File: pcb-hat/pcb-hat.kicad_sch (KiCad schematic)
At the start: 32 parts, among them U1 INA219AxD, U3 AOZ6605PI-1

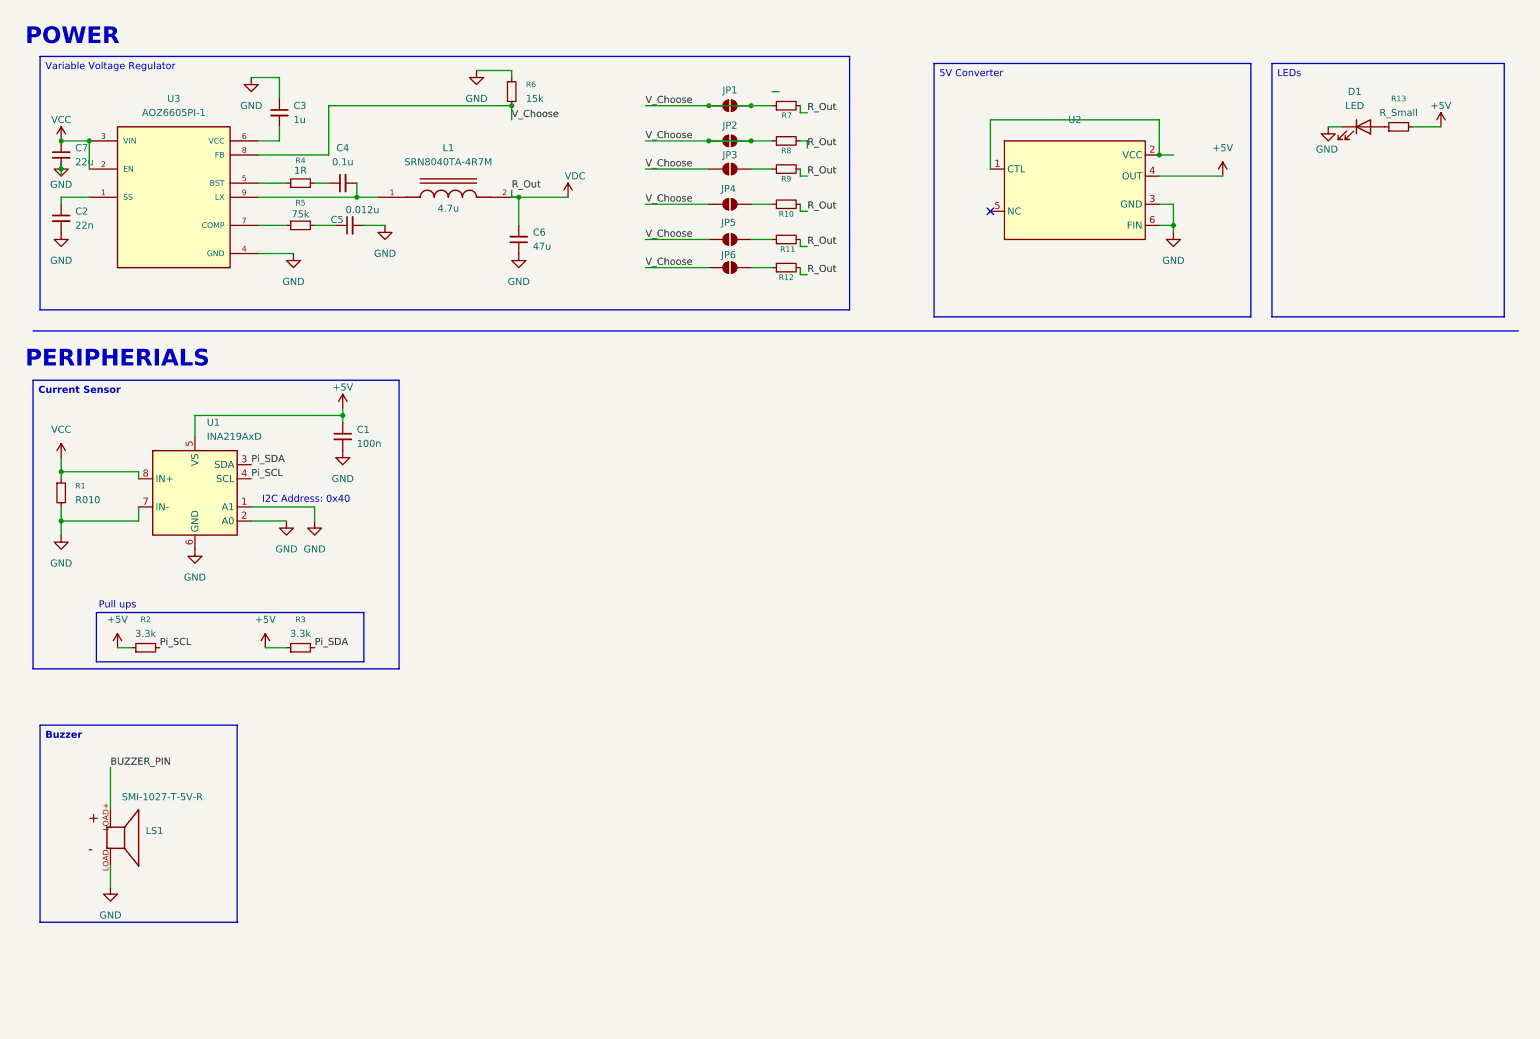
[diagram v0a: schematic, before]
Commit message: Add Pi, LED, Servo to the schematic
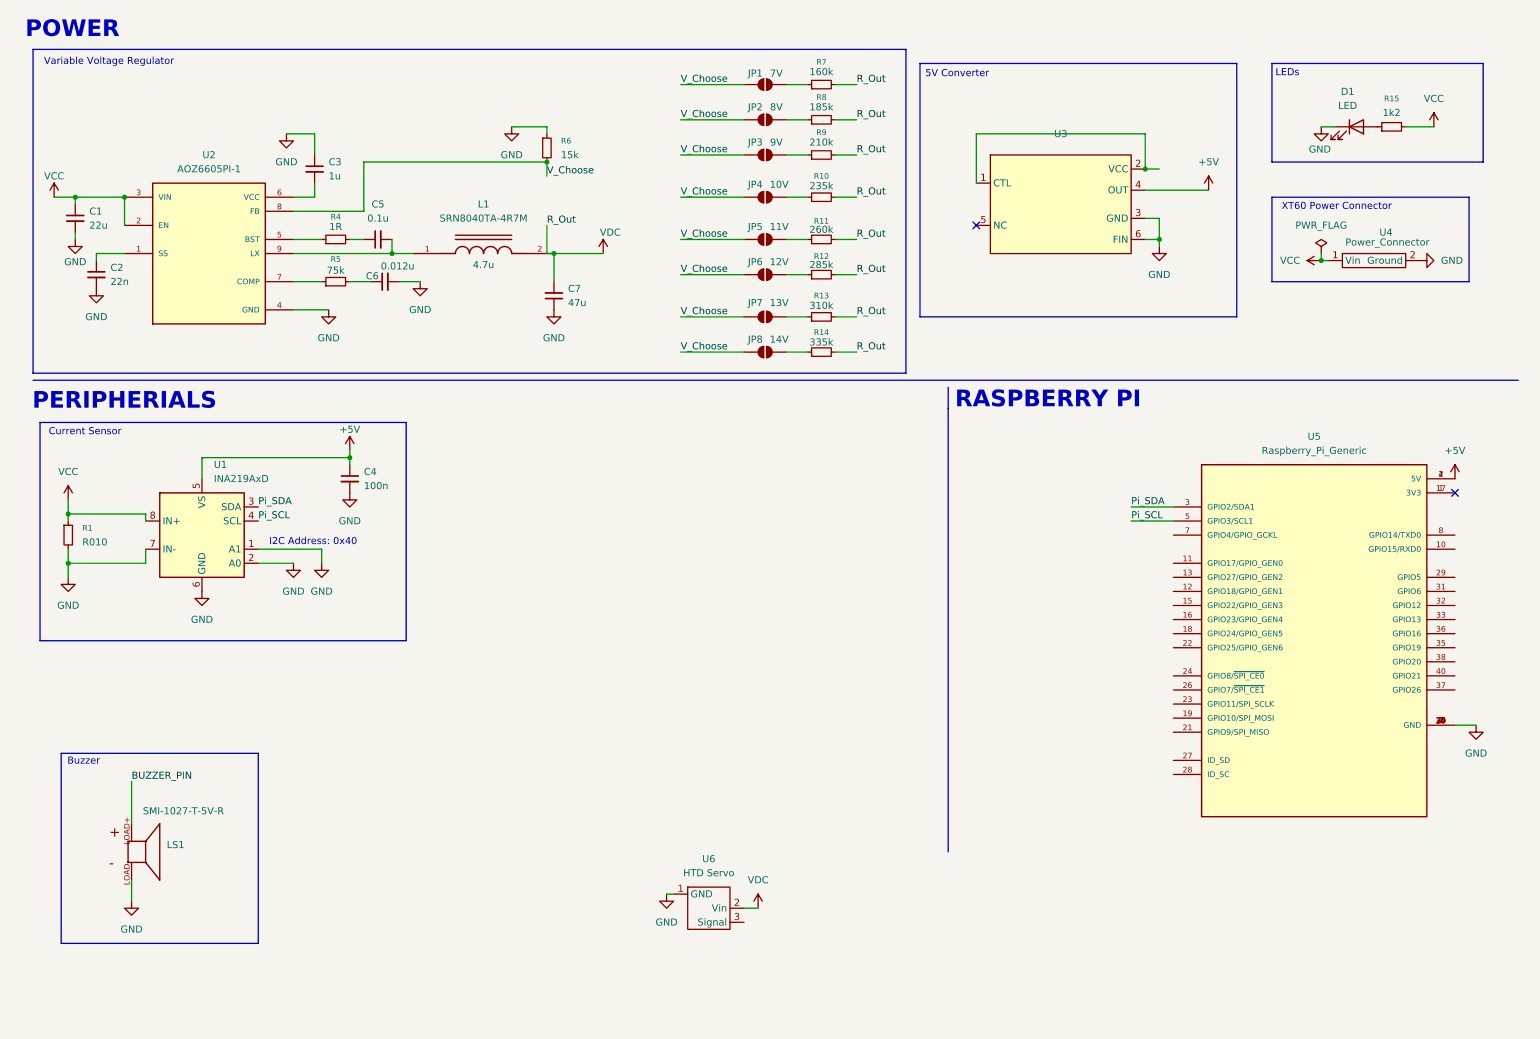
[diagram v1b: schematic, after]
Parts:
- removed R2, R3: 3.3k, Resistor_SMD:R_0603_1608Metric, symbol Device:R_Small
- added JP1, JP2: SolderJumper_2_Open, Jumper:SolderJumper-2_P1.3mm_Open_RoundedPad1.0x1.5mm, symbol Jumper:SolderJumper_2_Open
- added R7: 160k, Resistor_SMD:R_0201_0603Metric_Pad0.64x0.40mm_HandSolder, symbol Device:R_Small
- added R8: 185k, Resistor_SMD:R_0201_0603Metric_Pad0.64x0.40mm_HandSolder, symbol Device:R_Small
- added U4: Power_Connector, pi_hat:XT60, symbol PiHatComponents:XT60
- added U5: Raspberry_Pi_Generic, pcb_hat:Pi5Hat, symbol PiHatComponents:Raspberry_Pi_Generic
- added U6: HTD Servo, pcb_hat:Servo, symbol PiHatComponents:ServoPinHeader
- JP3: renamed from JP1; V_out (none) -> 9V
- JP4: renamed from JP2; V_out (none) -> 10V
- JP5: renamed from JP3; V_out (none) -> 11V
- JP6: renamed from JP4; V_out (none) -> 12V
- JP7: renamed from JP5; V_out (none) -> 13V
- JP8: renamed from JP6; V_out (none) -> 14V
- R15: renamed from R13; value R_Small -> 1k2
- renumbered C7 to C1, C1 to C4, C4 to C5, C5 to C6, C6 to C7, R8 to R10, R9 to R11, R10 to R12, R11 to R13, R12 to R14, R7 to R9, U3 to U2, U2 to U3
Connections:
- net +5V: now also U5.2 (5V), U5.4 (5V); no longer R15.2
- net GND: now also U4.2 (Ground), U5.20 (GND), U5.25 (GND), U5.30 (GND), U5.34 (GND), U5.39 (GND), U5.6 (GND), U5.9 (GND), U6.1 (GND)
- net Pi_SCL: now also U5.5 (GPIO3/SCL1)
- net Pi_SDA: now also U5.3 (GPIO2/SDA1)
- net VCC: now also R15.2, U4.1 (Vin)
- net VDC: now also R7.2, R8.2, U6.2 (Vin)
- net V_Choose: now also JP1.1 (A), JP2.1 (A); no longer JP3.2 (B), JP4.2 (B), R10.1, R9.1
- new net: JP4.2 (B), R10.1
- new net: U5.1 (3V3), U5.17 (3V3)
- new net: JP3.2 (B), R9.1
- new net: JP1.2 (B), R7.1
- new net: JP2.2 (B), R8.1
- no-connect marks 1 -> 2
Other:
- note added: "Buzzer"
- note added: "Current Sensor"
- note added: "LEDs"
- note added: "RASPBERRY PI"
- note added: "Variable Voltage Regulator"
- note added: "XT60 Power Connector"
- note removed: "Pull ups"
- moved on the sheet: C1, C2, C3, C4, C5, C6, C7, D1, JP3, JP4, JP5, JP6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

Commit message: Add new 5V regulator part, finish Servo connection
Also fix footprint of 7, 8, and 9V resistors to 0603 hand soldered
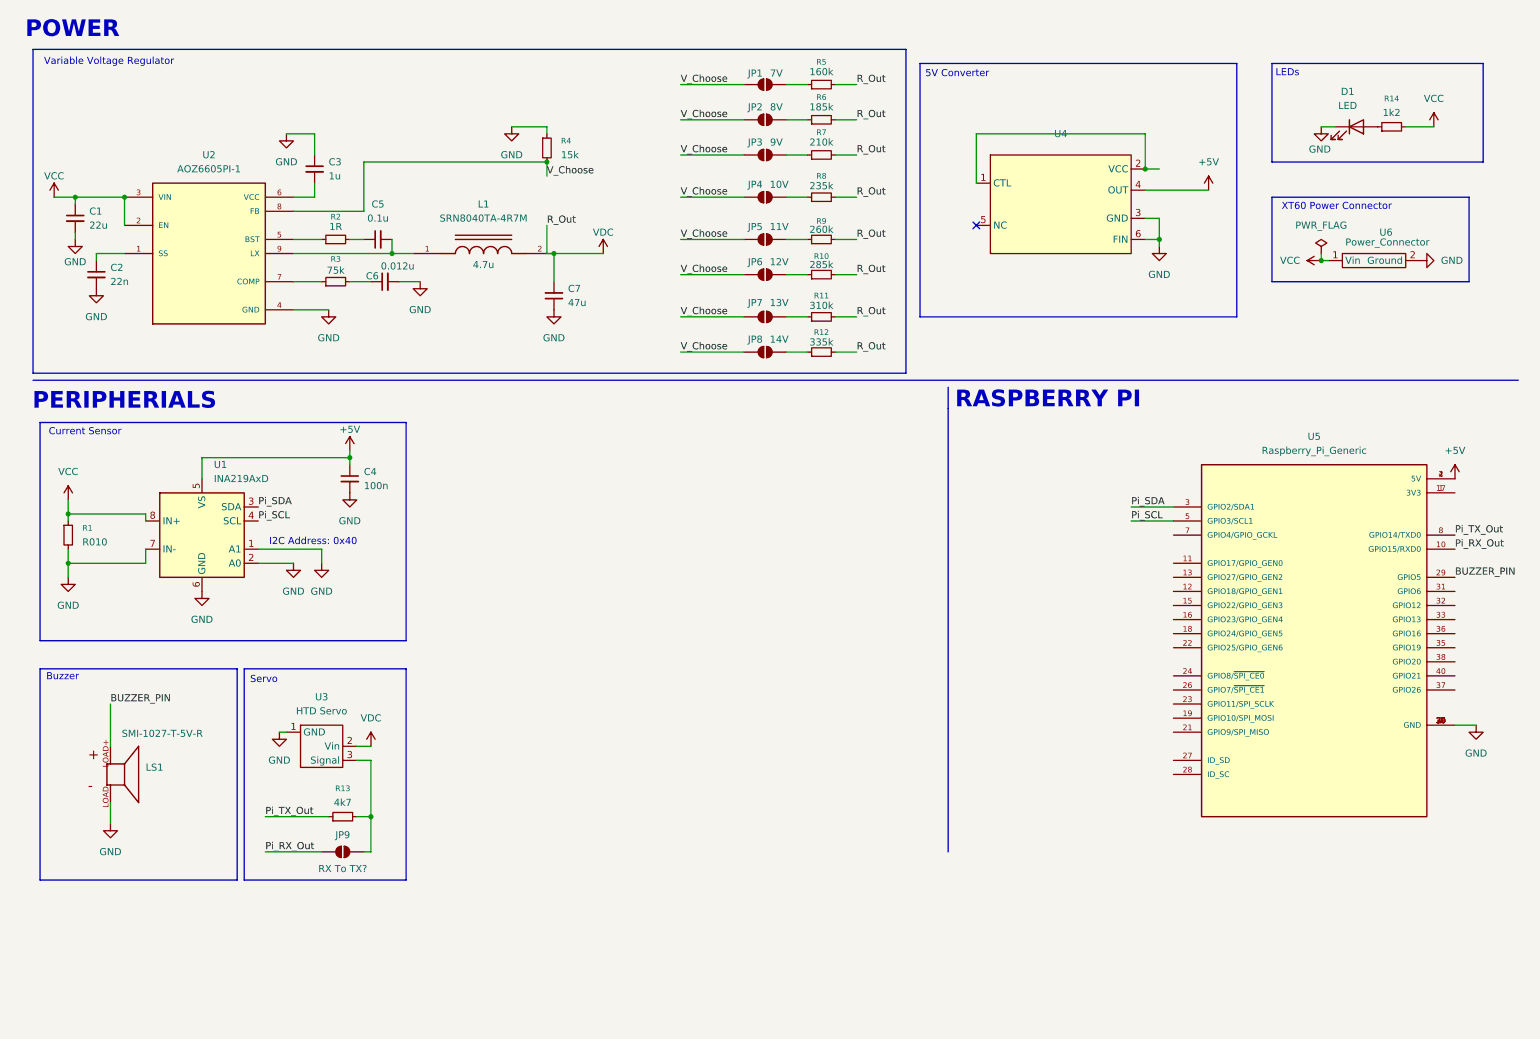
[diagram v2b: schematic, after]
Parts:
- added JP9: SolderJumper_2_Open, Jumper:SolderJumper-2_P1.3mm_Open_RoundedPad1.0x1.5mm, symbol Jumper:SolderJumper_2_Open
- added R13: 4k7, Resistor_SMD:R_0603_1608Metric_Pad0.98x0.95mm_HandSolder, symbol Device:R_Small
- R5: renamed from R7; footprint Resistor_SMD:R_0201_0603Metric_Pad0.64x0.40mm_HandSolder -> Resistor_SMD:R_0603_1608Metric_Pad0.98x0.95mm_HandSolder
- R6: renamed from R8; footprint Resistor_SMD:R_0201_0603Metric_Pad0.64x0.40mm_HandSolder -> Resistor_SMD:R_0603_1608Metric_Pad0.98x0.95mm_HandSolder
- R7: renamed from R9; footprint Resistor_SMD:R_0201_0603Metric_Pad0.64x0.40mm_HandSolder -> Resistor_SMD:R_0603_1608Metric_Pad0.98x0.95mm_HandSolder
- renumbered R12 to R10, R13 to R11, R14 to R12, R15 to R14, R4 to R2, R5 to R3, R6 to R4, R10 to R8, R11 to R9, U6 to U3, U3 to U4, U4 to U6
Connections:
- net BUZZER_PIN: now also U5.29 (GPIO5)
- net Pi_RX_Out: now reaches U5.10 (GPIO15/RXD0)
- net Pi_RX_Out: now also JP9.1 (A)
- net Pi_TX_Out: now reaches U5.8 (GPIO14/TXD0)
- net Pi_TX_Out: now also R13.1
- net at U3.3 (Signal): now also JP9.2 (B), R13.2
- no-connect marks 2 -> 1
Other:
- note added: "Servo"
- moved on the sheet: LS1, U3

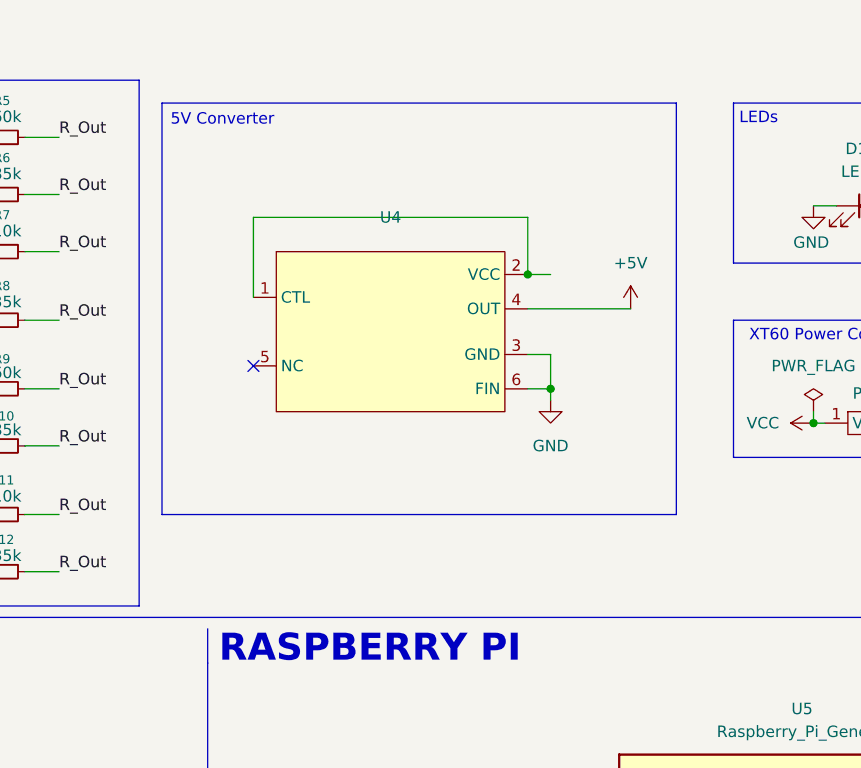
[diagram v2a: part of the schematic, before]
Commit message: Update pcb-hat.kicad_sch
replaced 5v regulator
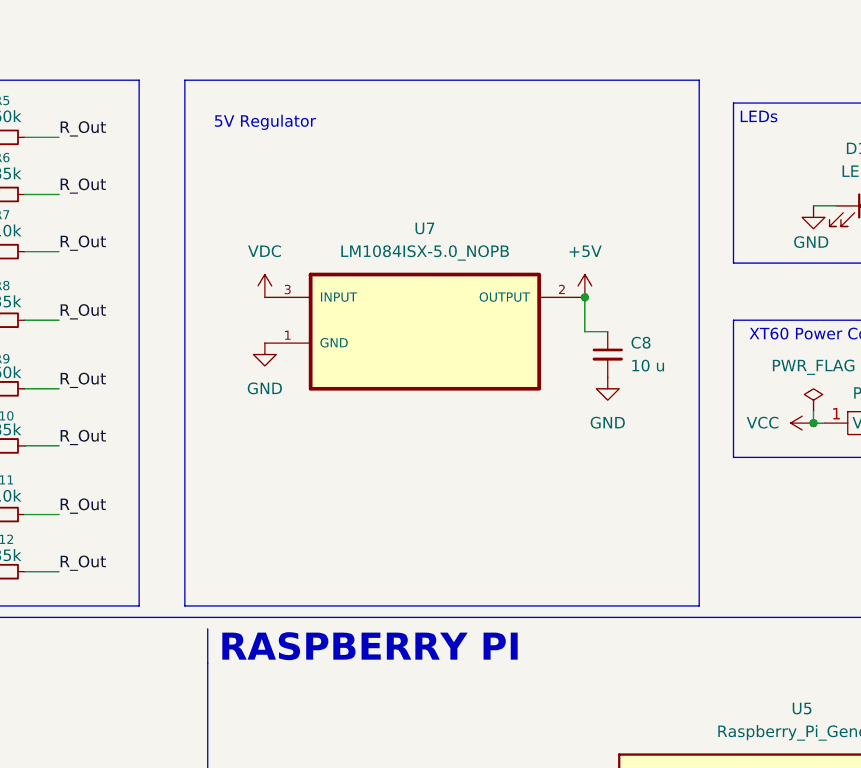
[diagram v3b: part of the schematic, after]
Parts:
- removed U4: ~, pcb_hat:DPAK172P1054X200-6N, symbol PiHatComponents:BA50DD0WHFP-TR-HRP-5
- added C8: 10 u, symbol Device:C_Small
- added U7: LM1084ISX-5.0_NOPB, LM1084ISX-5.0_NOPB:TO254P1524X483-4N, symbol PiHatComponents:LM1084ISX-5.0_NOPB
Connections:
- net +5V: now also C8.1, U7.2 (OUTPUT), U7.4 (OUTPUT)
- net GND: now also C8.2, U7.1 (GND)
- net VDC: now also U7.3 (INPUT)
- no-connect marks 1 -> 0
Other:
- note added: "5V Regulator"

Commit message: WIP: Add breakouts to schematic
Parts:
- added U4: Vertical_Pi_Breakout, symbol PiHatComponents:vertical_pi_breakout
- added U8: Horizontal_Pi_Breakout, symbol PiHatComponents:horizontal_pi_breakout
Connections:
- net Pi_SCL: now also U4.2 (GPIO3)
- net Pi_SDA: now also U4.1 (GPIO2)
- net GPIO4: now reaches U5.7 (GPIO4/GPIO_GCKL)
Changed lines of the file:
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@@
 	(polyline
 		(pts
-			(xy 179.07 83.82) (xy 179.07 163.83)
+			(xy 129.54 83.82) (xy 129.54 163.83)
 		)
 		(stroke
@@
 	(polyline
 		(pts
-			(xy 179.07 80.01) (xy 179.07 83.82)
+			(xy 129.54 80.01) (xy 129.54 83.82)
 		)
 		(stroke
@@
 		)
 	)
+	(label "GPIO4"
+		(at 219.71 106.68 0)
+		(effects
+			(font
+				(size 1.27 1.27)
+			)
+			(justify left bottom)
+		)
+	)
 	(label "Pi_SCL"
 		(at 54.61 104.14 0)
@@
 		)
 	)
+	(label "Pi_SCL"
+		(at 154.94 97.79 0)
+		(effects
+			(font
+				(size 1.27 1.27)
+			)
+			(justify left bottom)
+		)
+	)
 	(label "Pi_SDA"
 		(at 54.61 101.6 0)
@@
 		)
 	)
+	(label "Pi_SDA"
+		(at 154.94 93.98 0)
+		(effects
+			(font
+				(size 1.27 1.27)
+			)
+			(justify left bottom)
+		)
+	)
 	(label "R_Out"
 		(at 106.68 50.8 0)
@@
 	)
 	(symbol
+		(lib_id "PiHatComponents:vertical_pi_breakout")
+		(at 147.32 86.36 0)
+		(unit 1)
+		(exclude_from_sim no)
+		(in_bom yes)
+		(on_board yes)
+		(dnp no)
+		(fields_autoplaced yes)
+		(property "Reference" "U4"
+			(at 147.32 86.36 0)
+			(effects
+				(font
+					(size 1.27 1.27)
+				)
+			)
+		)
+		(property "Value" "Vertical_Pi_Breakout"
+			(at 147.32 88.9 0)
+			(effects
+				(font
+					(size 1.27 1.27)
+				)
+			)
+		)
+		(property "Footprint" ""
+			(at 147.32 86.36 0)
+			(effects
+				(font
+					(size 1.27 1.27)
+				)
+				(hide yes)
+			)
+		)
+		(property "Datasheet" ""
+			(at 147.32 86.36 0)
+			(effects
+				(font
+					(size 1.27 1.27)
+				)
+				(hide yes)
+			)
+		)
+		(property "Description" ""
+			(at 147.32 86.36 0)
+			(effects
+				(font
+					(size 1.27 1.27)
+				)
+				(hide yes)
+			)
+		)
+		(pin "9"
+		)
+		(pin "4"
+		)
+		(pin "2"
+		)
+		(pin "6"
+		)
+		(pin "7"
+		)
+		(pin "5"
+		)
+		(pin "1"
+		)
+		(pin "3"
+		)
+		(pin "13"
+		)
+		(pin "10"
+		)
+		(pin "8"
+		)
+		(pin "17"
+		)
+		(pin "12"
+		)
+		(pin "16"
+		)
+		(pin "14"
+		)
+		(pin "15"
+		)
+		(pin "11"
+		)
+		(instances
+			(project ""
+				(path "/a3c2d30d-0751-4de7-a899-3d89ad40795d"
+					(reference "U4")
+					(unit 1)
+				)
+			)
+		)
+	)
+	(symbol
 		(lib_id "power:GND")
 		(at 185.42 48.26 0)
@@
 					(unit 1)
 				)
+			)
+		)
+	)
+	(symbol
+		(lib_id "PiHatComponents:horizontal_pi_breakout")
+		(at 198.12 125.73 270)
+		(unit 1)
+		(exclude_from_sim no)
+		(in_bom yes)
+		(on_board yes)
+		(dnp no)
+		(fields_autoplaced yes)
+		(property "Reference" "U8"
+			(at 174.625 85.09 90)
+			(effects
+				(font
+					(size 1.27 1.27)
+				)
+			)
+		)
+		(property "Value" "Horizontal_Pi_Breakout"
+			(at 174.625 87.63 90)
+			(effects
+				(font
+					(size 1.27 1.27)
+				)
+			)
+		)
+		(property "Footprint" ""
+			(at 198.12 125.73 0)
+			(effects
+				(font
+					(size 1.27 1.27)
+				)
+				(hide yes)
+			)
+		)
+		(property "Datasheet" ""
+			(at 198.12 125.73 0)
+			(effects
+				(font
+					(size 1.27 1.27)
+				)
+				(hide yes)
+			)
+		)
+		(property "Description" ""
+			(at 198.12 125.73 0)
+			(effects
+				(font
+					(size 1.27 1.27)
+				)
+				(hide yes)
+			)
+		)
+		(pin "2"
+		)
+		(pin "9"
+		)
+		(pin "5"
+		)
+		(pin "11"
+		)
+		(pin "4"
+		)
+		(pin "7"
+		)
+		(pin "13"
+		)
+		(pin "18"
+		)
+		(pin "17"
+		)
+		(pin "15"
+		)
+		(pin "16"
+		)
+		(pin "3"
+		)
+		(pin "14"
+		)
+		(pin "12"
+		)
+		(pin "10"
+		)
+		(pin "8"
+		)
+		(pin "6"
+		)
+		(pin "1"
+		)
+		(instances
+			(project ""
+				(path "/a3c2d30d-0751-4de7-a899-3d89ad40795d"
+					(reference "U8")
+					(unit 1)
+				)
